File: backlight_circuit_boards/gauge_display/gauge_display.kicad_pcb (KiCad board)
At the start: 2 copper layers, 40 x 18 mm, 8 parts, among them J1 Conn_01x03, J2 Conn_01x03

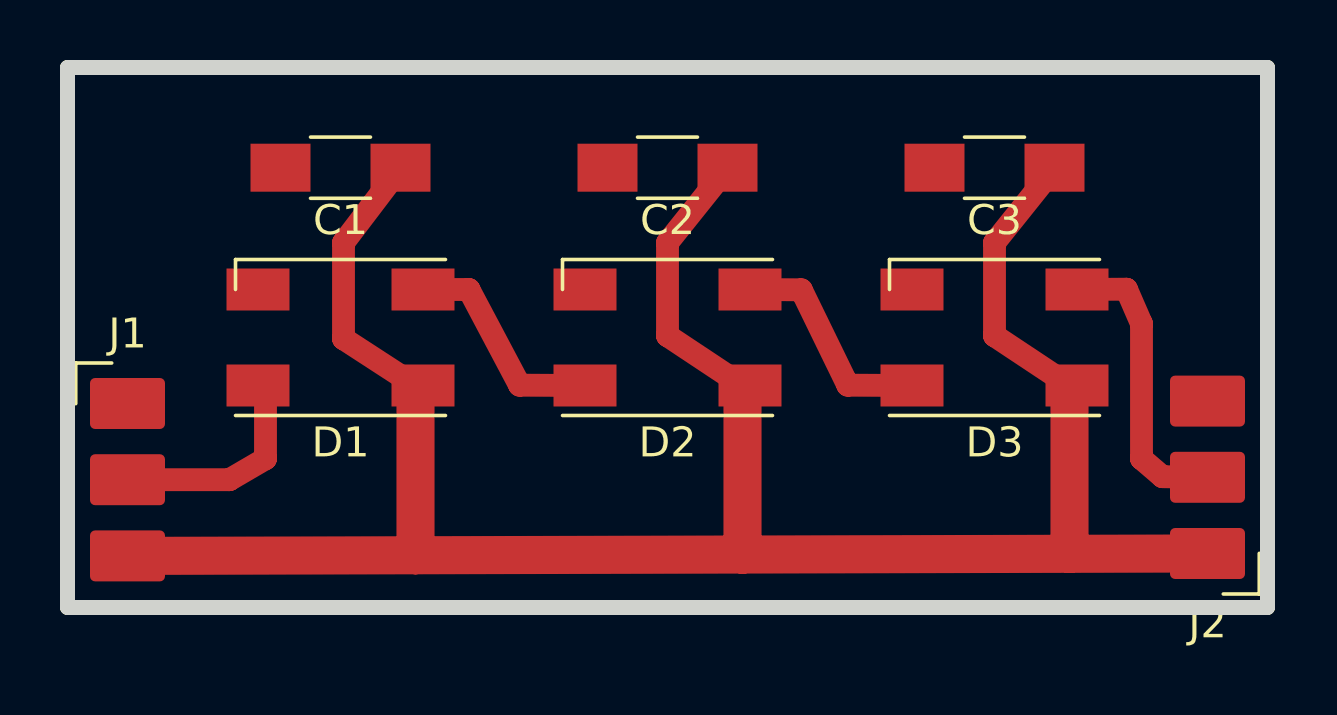
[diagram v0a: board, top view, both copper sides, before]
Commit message: Make clock/km board a little smaller, built combined artwork SVG
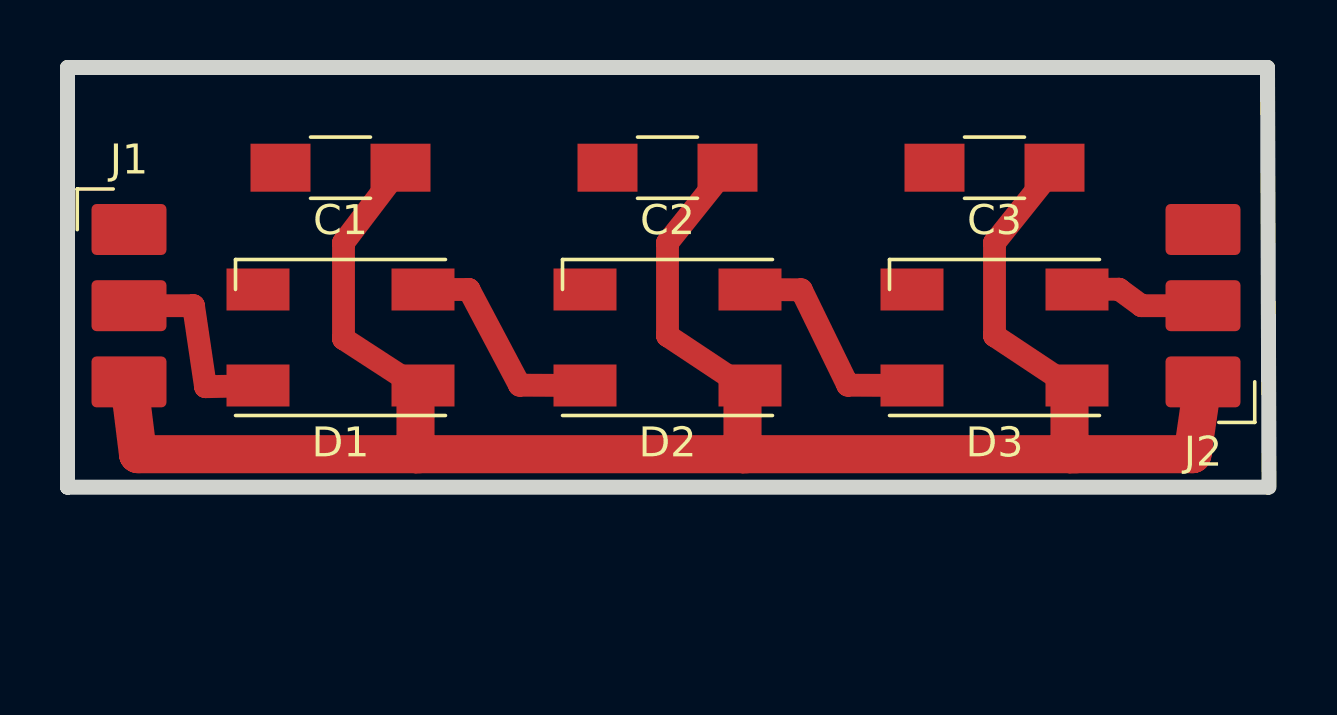
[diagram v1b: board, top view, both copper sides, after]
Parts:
- moved J1 5.80 mm to (24.1, 30.4)
- moved J2 5.72 mm to (60.0, 35.5)
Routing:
- net VCC: track 80.7 -> 75.2 mm
- net Net-(D3-Pad2): track 10.1 -> 4.63 mm
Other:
- board size 40 x 18 mm -> 40 x 14 mm
